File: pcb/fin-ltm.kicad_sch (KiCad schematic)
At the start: 50 parts, among them J1 Connector, USB-TYPE-C-16P, J2 Test Connector, Q1 MMBT3904, Q2 HL3415A, U1 ESP32-C3FH4, U3 SN74LV1T34DBV, X1 40MHz, 15pF

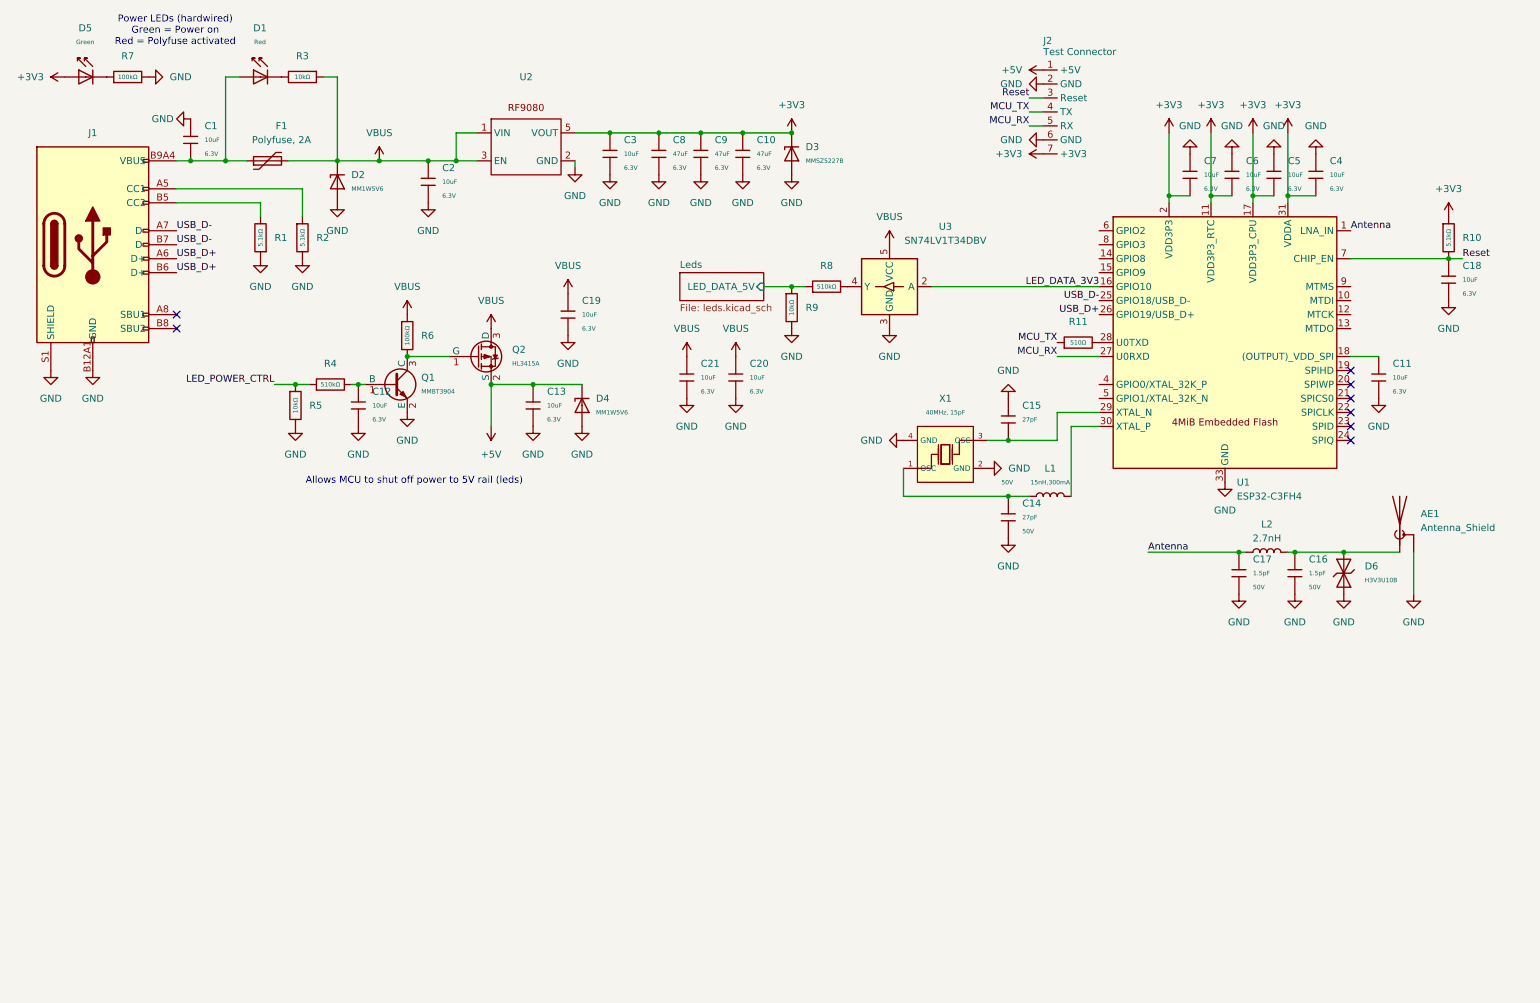
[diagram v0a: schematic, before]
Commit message: schematic update
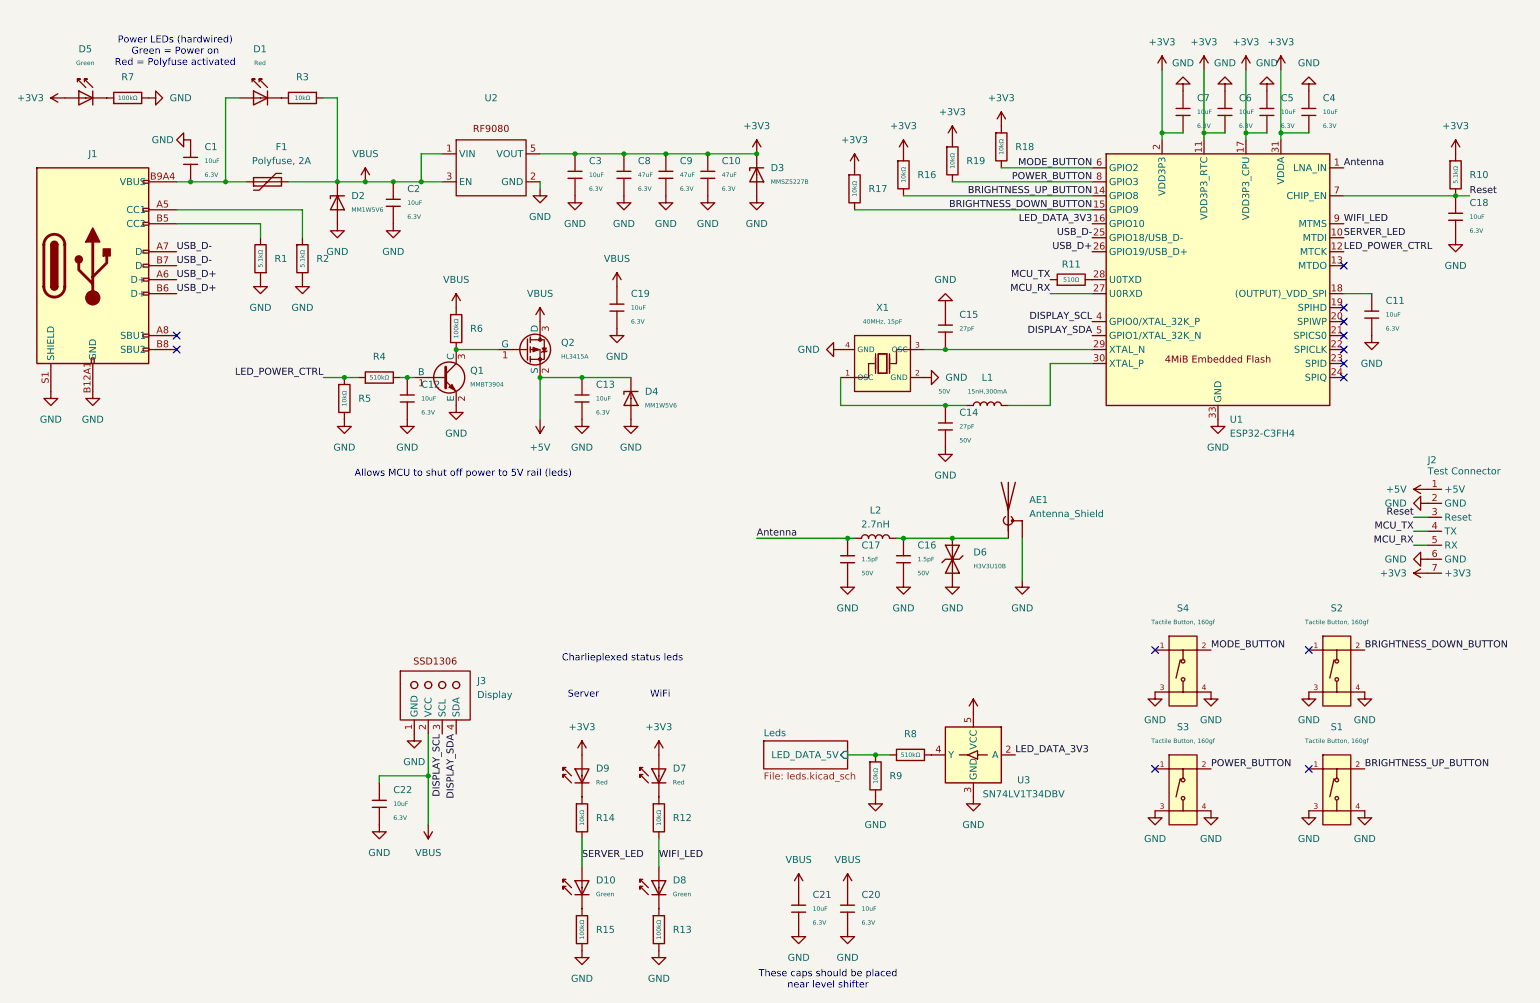
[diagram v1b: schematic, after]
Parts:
- added C22: 10uF, PCM_JLCPCB:C_0402, symbol PCM_JLCPCB-Capacitors:0402,10uF
- added D10, D8: Green, PCM_JLCPCB:D_0805, symbol PCM_JLCPCB-Diodes:LED,0805,Green
- added D7, D9: Red, PCM_JLCPCB:D_0805, symbol PCM_JLCPCB-Diodes:LED,0805,Red
- added J3: Display, symbol New_Library:SSD1306_Conn
- added R12, R14, R16, R17, R18, R19: 10kΩ, PCM_JLCPCB:R_0402, symbol PCM_JLCPCB-Resistors:0402,10kΩ
- added R13, R15: 100kΩ, PCM_JLCPCB:R_0402, symbol PCM_JLCPCB-Resistors:0402,100kΩ
- added S1, S2, S3, S4: Tactile Button, 160gf, PCM_JLCPCB:SW-SMD_4P-L5.1-W5.1-P3.70-LS6.5-TL-2, symbol PCM_JLCPCB-Connectors_Buttons:Tactile Button, 160gf, 12V, 50mA, 5.1mm
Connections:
- net +3V3: now also D7.2, D9.2, R16.1, R17.1, R18.1, R19.1
- net GND: now also C22.2, J3.1 (GND), R13.2, R15.2, S1.3 (C), S1.4 (D), S2.3 (C), S2.4 (D), S3.3 (C), S3.4 (D), S4.3 (C), S4.4 (D)
- net LED_POWER_CTRL: now also U1.12 (MTCK)
- net VBUS: now also C22.1, J3.2 (VCC)
- net SERVER_LED: now reaches U1.10 (MTDI)
- net SERVER_LED: now also D10.2, R14.2
- net BRIGHTNESS_UP_BUTTON: now reaches U1.14 (GPIO8)
- net BRIGHTNESS_UP_BUTTON: now also R16.2, S1.2 (B)
- net BRIGHTNESS_DOWN_BUTTON: now reaches U1.15 (GPIO9)
- net BRIGHTNESS_DOWN_BUTTON: now also R17.2, S2.2 (B)
- net DISPLAY_SCL: now reaches U1.4 (GPIO0/XTAL_32K_P)
- net DISPLAY_SCL: now also J3.3 (SCL)
- net DISPLAY_SDA: now reaches U1.5 (GPIO1/XTAL_32K_N)
- net DISPLAY_SDA: now also J3.4 (SDA)
- net MODE_BUTTON: now reaches U1.6 (GPIO2)
- net MODE_BUTTON: now also R18.2, S4.2 (B)
- net POWER_BUTTON: now reaches U1.8 (GPIO3)
- net POWER_BUTTON: now also R19.2, S3.2 (B)
- net WIFI_LED: now reaches U1.9 (MTMS)
- net WIFI_LED: now also D8.2, R12.2
- new net: D8.1, R13.1
- new net: D9.1, R14.1
- new net: D7.1, R12.1
- new net: D10.1, R15.1
- no-connect marks 8 -> 13
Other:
- note added: "Charlieplexed status leds"
- note added: "Server"
- note added: "These caps should be placed near level shifter"
- note added: "WiFi"
- moved on the sheet: AE1, C1, C10, C11, C12, C13, C14, C15, C16, C17, C18, C19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

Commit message: BOM check and small tweaks
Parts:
- J2, J3: now left out of the parts list
- U2: value ~ -> RT9080; LCSC (none) -> C841192
- U3: LCSC (none) -> C100024
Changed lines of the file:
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@@
 		(unit 1)
 		(exclude_from_sim no)
-		(in_bom yes)
+		(in_bom no)
 		(on_board yes)
 		(dnp no)
@@
 		(unit 1)
 		(exclude_from_sim no)
-		(in_bom yes)
+		(in_bom no)
 		(on_board yes)
 		(dnp no)
@@
 			)
 		)
+		(property "LCSC" "C100024"
+			(at 186.69 147.32 0)
+			(effects
+				(font
+					(size 1.27 1.27)
+				)
+				(hide yes)
+			)
+		)
 		(pin "5"
 		)
@@
 			)
 		)
-		(property "Value" "~"
+		(property "Value" "RT9080"
 			(at 99.06 30.48 0)
 			(effects
@@
 			(at 99.06 40.64 0)
 			(effects
+				(font
+					(size 1.27 1.27)
+				)
+				(hide yes)
+			)
+		)
+		(property "LCSC" " C841192 "
+			(at 99.06 40.64 0)
+			(effects

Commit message: Started adding leds and started making pcbs.
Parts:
- removed R9: 10kΩ, PCM_JLCPCB:R_0402, symbol PCM_JLCPCB-Resistors:0402,10kΩ
- added R9: 100kΩ, PCM_JLCPCB:R_0402, symbol PCM_JLCPCB-Resistors:0402,100kΩ
- AE1: footprint (none) -> Library:Inverted_F_Antenna_2.4Ghz_1.0mmPCB_TI_CC2430DB.pretty
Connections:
- net GND: now also R9.2
- net Leds/LED_DATA_5V: now also R9.1

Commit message: more pcb routing
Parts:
- J2: footprint (none) -> Library:Test_connector
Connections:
- net MCU_RX: now also J2.4 (TX); no longer J2.5 (RX)
- net MCU_TX: now also J2.5 (RX); no longer J2.4 (TX)
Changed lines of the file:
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@@
 		)
 	)
-	(label "MCU_RX"
+	(label "MCU_TX"
 		(at 266.7 109.22 180)
 		(effects
@@
 		)
 	)
-	(label "MCU_TX"
+	(label "MCU_RX"
 		(at 266.7 106.68 180)
 		(effects
@@
 			)
 		)
-		(property "Footprint" ""
+		(property "Footprint" "Library:Test_connector"
 			(at 269.24 106.68 0)
 			(hide yes)

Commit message: pcb
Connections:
- net BRIGHTNESS_DOWN_BUTTON: now also U1.16 (GPIO10); no longer U1.15 (GPIO9)
- net BRIGHTNESS_UP_BUTTON: now also U1.15 (GPIO9); no longer U1.14 (GPIO8)
- net DISPLAY_SCL: now also R18.2
- net DISPLAY_SDA: now also R19.2
- net LED_DATA_3V3: now also U1.14 (GPIO8); no longer U1.16 (GPIO10)
- net MODE_BUTTON: no longer R18.2
- net POWER_BUTTON: no longer R19.2
- net SERVER_LED: now also U1.9 (MTMS); no longer U1.10 (MTDI)
- net WIFI_LED: now also U1.10 (MTDI); no longer U1.9 (MTMS)
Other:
- moved on the sheet: AE1, C14, C15, C16, C17, D6, L1, L2, R16, R17, X1

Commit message: pcb
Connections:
- net DISPLAY_SCL: now also R19.2, U1.5 (GPIO1/XTAL_32K_N); no longer R18.2, U1.4 (GPIO0/XTAL_32K_P)
- net DISPLAY_SDA: now also R18.2, U1.4 (GPIO0/XTAL_32K_P); no longer R19.2, U1.5 (GPIO1/XTAL_32K_N)
